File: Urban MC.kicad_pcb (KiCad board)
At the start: 4 copper layers, 167 x 104 mm, 79 parts, among them J1 Conn_01x02, J2 Conn_01x02, J3 Conn_01x03, J3 Screw_Terminal_01x02, J4 Conn_01x02, J4 Screw_Terminal_01x01, J5 Screw_Terminal_01x01, Q1 IQE022N06LM5CGSCATMA1, Q10 IQE022N06LM5CGSCATMA1, Q11 IQE022N06LM5CGSCATMA1, Q12 IQE022N06LM5CGSCATMA1, Q13 IQE022N06LM5CGSCATMA1, Q14 IQE022N06LM5CGSCATMA1, Q15 IQE022N06LM5CGSCATMA1, Q16 IQE022N06LM5CGSCATMA1, Q17 IQE022N06LM5CGSCATMA1, Q18 IQE022N06LM5CGSCATMA1, Q19 IQE022N06LM5CGSCATMA1, Q2 IQE022N06LM5CGSCATMA1, Q20 IQE022N06LM5CGSCATMA1, Q21 IQE022N06LM5CGSCATMA1, Q22 IQE022N06LM5CGSCATMA1, Q23 IQE022N06LM5CGSCATMA1, Q24 IQE022N06LM5CGSCATMA1, Q3 IQE022N06LM5CGSCATMA1, Q4 IQE022N06LM5CGSCATMA1, Q5 IQE022N06LM5CGSCATMA1, Q6 IQE022N06LM5CGSCATMA1, Q7 IQE022N06LM5CGSCATMA1, Q8 IQE022N06LM5CGSCATMA1, Q9 IQE022N06LM5CGSCATMA1, SW1 CAN_TERM, SW2 SW_Push, U1 MCP2561/2, U12 TJA1050, U2 MCP4725, U3 MCP2515-xSO, Y1 8MHz

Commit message: ready for mosfet feedback
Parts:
- removed the J2 at (137.7, 82.9)
- removed the J2 at (38.5, 151.0)
- removed the J3 at (58.3, 167.7)
- removed the J4 at (113.3, -58.2)
- removed the J4 at (102.4, 93.8)
- removed J5: Screw_Terminal_01x01, urban_mc_custom_footprints:WP-SHFU_7461100
- removed U12: TJA1050, Package_SO:SOIC-8_3.9x4.9mm_P1.27mm
- added J2: Conn_01x02, urban_mc_custom_footprints:CON_436500200_MOL, F.Cu at (116.8, 73.5)
- added J4: Conn_01x02, urban_mc_custom_footprints:TE_1-1986660-2, F.Cu at (95.2, 118.1)
- moved U4 210.6 mm to (102.9, 149.9)
- moved D4 204.6 mm to (105.4, 135.9)
- moved C14 203.7 mm to (121.0, 141.0)
- moved C15 202.4 mm to (121.9, 145.2)
- moved C16 202.4 mm to (121.9, 148.6)
- moved J1 154.1 mm to (127.0, 57.0)
- moved C5 94.1 mm to (212.1, 64.8)
- moved Q1 88.8 mm to (185.6, 62.3)
- moved Q3 88.8 mm to (191.7, 62.3)
- moved Q5 88.8 mm to (197.9, 62.3)
- moved Q7 88.8 mm to (204.0, 62.3)
- moved Q6 88.2 mm to (197.7, 69.8)
- moved Q8 88.2 mm to (203.9, 69.8)
- moved Q2 88.2 mm to (185.4, 69.8)
- moved Q4 88.2 mm to (191.6, 69.8)
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
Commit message: symbol changes and filled zone solution, still looking for more feedback
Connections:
- U3 pad 14: SI -> CS
- U3 pad 16: CS -> SI
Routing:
- net Net-(Q21-GATE): track 81.2 -> 79.7 mm

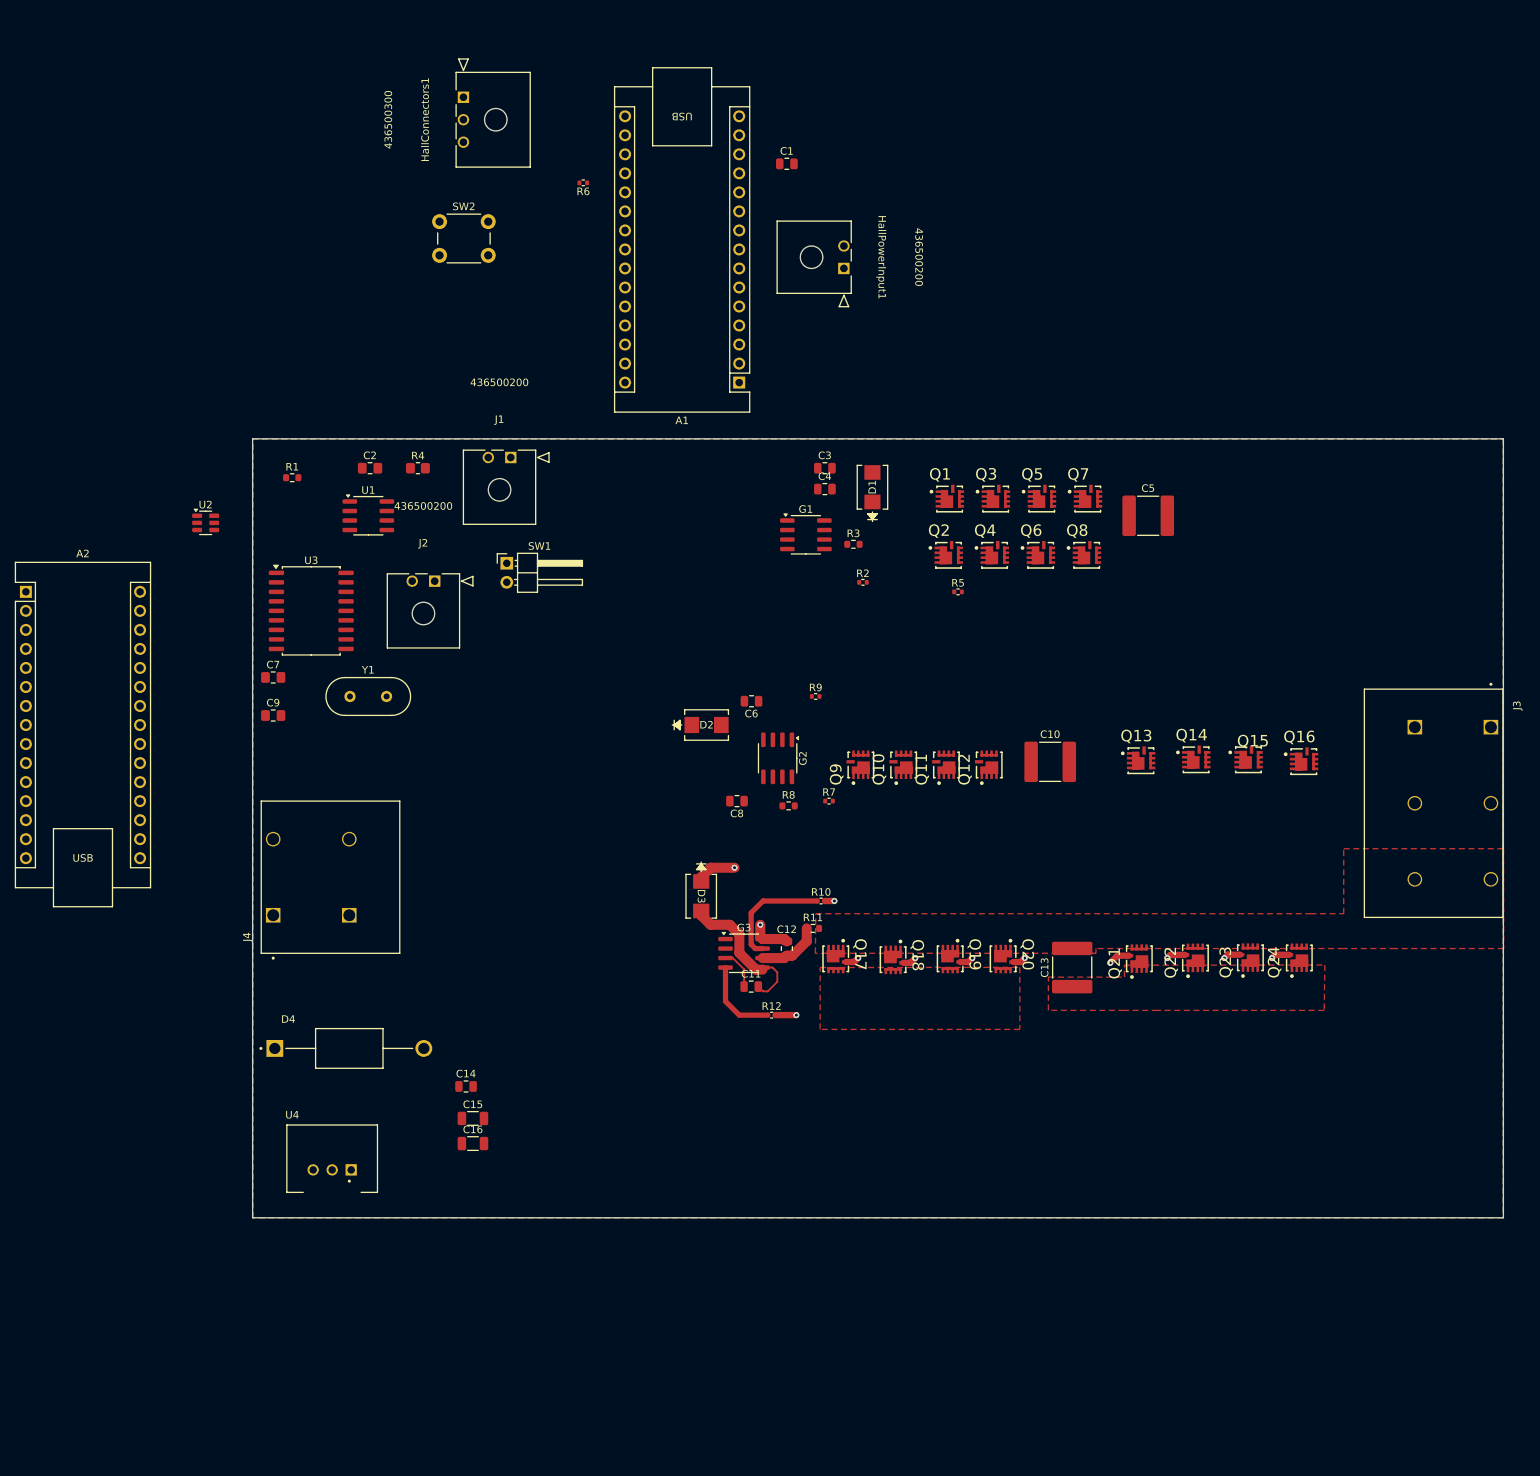
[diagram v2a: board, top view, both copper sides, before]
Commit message: duplicated mosfet section with connected filled zones
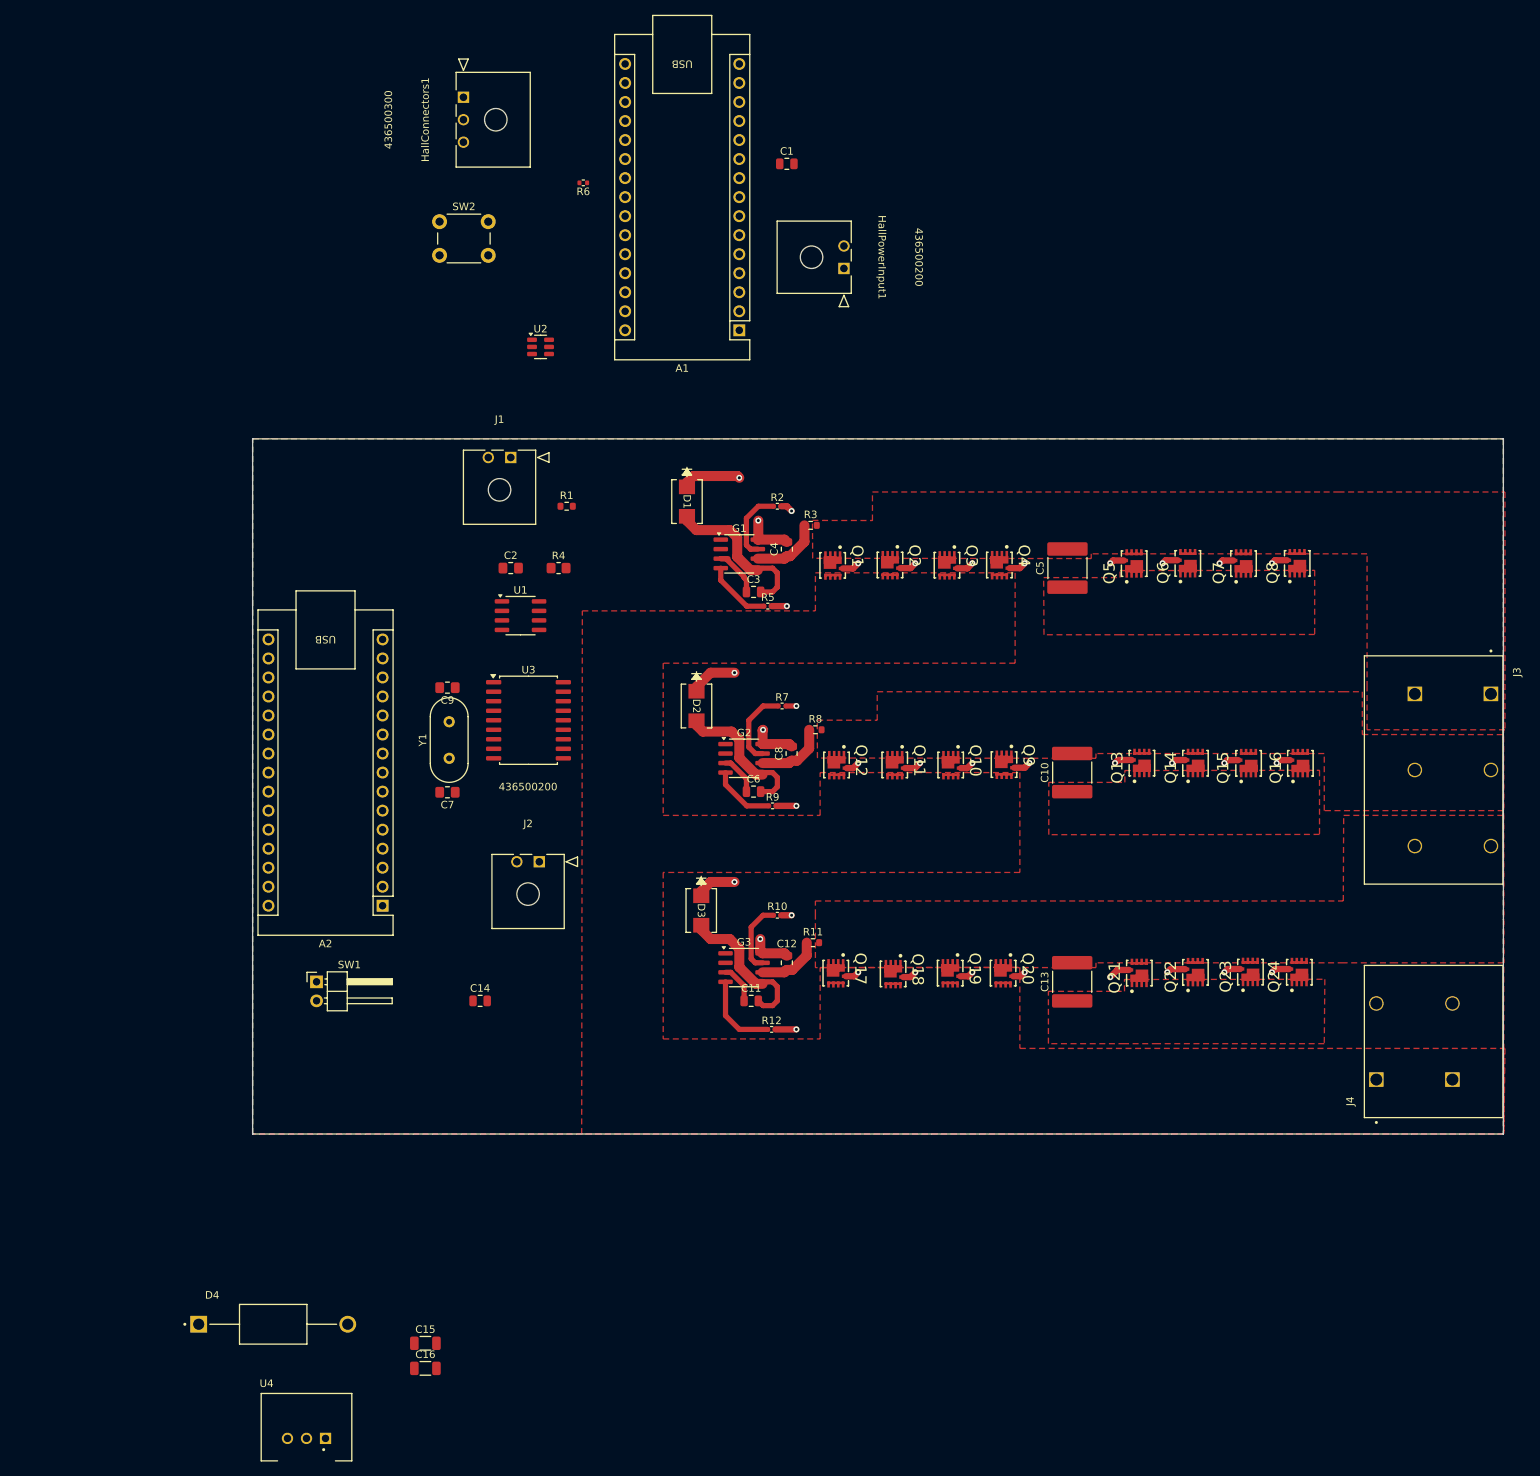
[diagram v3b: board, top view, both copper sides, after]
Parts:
- moved J4 148.9 mm to (242.5, 140.0)
- moved A2 63.4 mm to (109.9, 116.8), turned to 180 degrees
- moved SW1 61.4 mm to (101.0, 127.0)
- moved U2 50.5 mm to (130.9, 42.2)
- moved J2 40.0 mm to (130.8, 111.0)
- moved D4 38.2 mm to (95.2, 172.7)
- moved R1 36.8 mm to (134.4, 63.5)
- moved U4 36.0 mm to (99.4, 185.7)
- moved U3 32.5 mm to (129.3, 92.1)
- moved C16 30.7 mm to (115.6, 178.6)
- moved C15 30.7 mm to (115.6, 175.3)
- moved Q8 27.9 mm to (231.8, 71.1), turned to 90 degrees
- moved C7 27.9 mm to (118.5, 101.7), turned to 180 degrees
- moved R5 25.5 mm to (161.3, 76.8)
- moved D1 24.8 mm to (150.5, 62.9), turned to -90 degrees
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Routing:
- net Net-(Q5-GATE): track 0.00 -> 79.4 mm, vias 0 -> 5
- net Net-(Q13-GATE): track 0.00 -> 79.3 mm, vias 0 -> 5
- net Net-(Q10-GATE): track 0.00 -> 46.8 mm, vias 0 -> 5
- net Net-(Q1-GATE): track 0.00 -> 46.7 mm, vias 0 -> 5
- net +12V: track 20.1 -> 61.6 mm
- net Net-(G2-VB): track 0.00 -> 21.6 mm, vias 0 -> 2
- net Net-(G1-VB): track 0.00 -> 21.4 mm, vias 0 -> 2
- net GND: track 5.41 -> 17.9 mm
- net Net-(G2-HO): track 0.00 -> 10.5 mm
- net Net-(G1-HO): track 0.00 -> 9.61 mm
- net Net-(G2-VS): track 0.00 -> 9.53 mm
- net Net-(G1-VS): track 0.00 -> 9.35 mm
- net Net-(G1-LO): track 0.00 -> 8.82 mm
- net Net-(G2-LO): track 0.00 -> 8.56 mm
- net Net-(Q17-GATE): track 39.7 -> 45.9 mm
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- added copper zone on F.Cu, net Net-(J3-Pin_1)
- added copper zone on F.Cu, net Net-(J3-Pin_2)
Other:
- board size 167 x 104 mm -> 167 x 92.8 mm

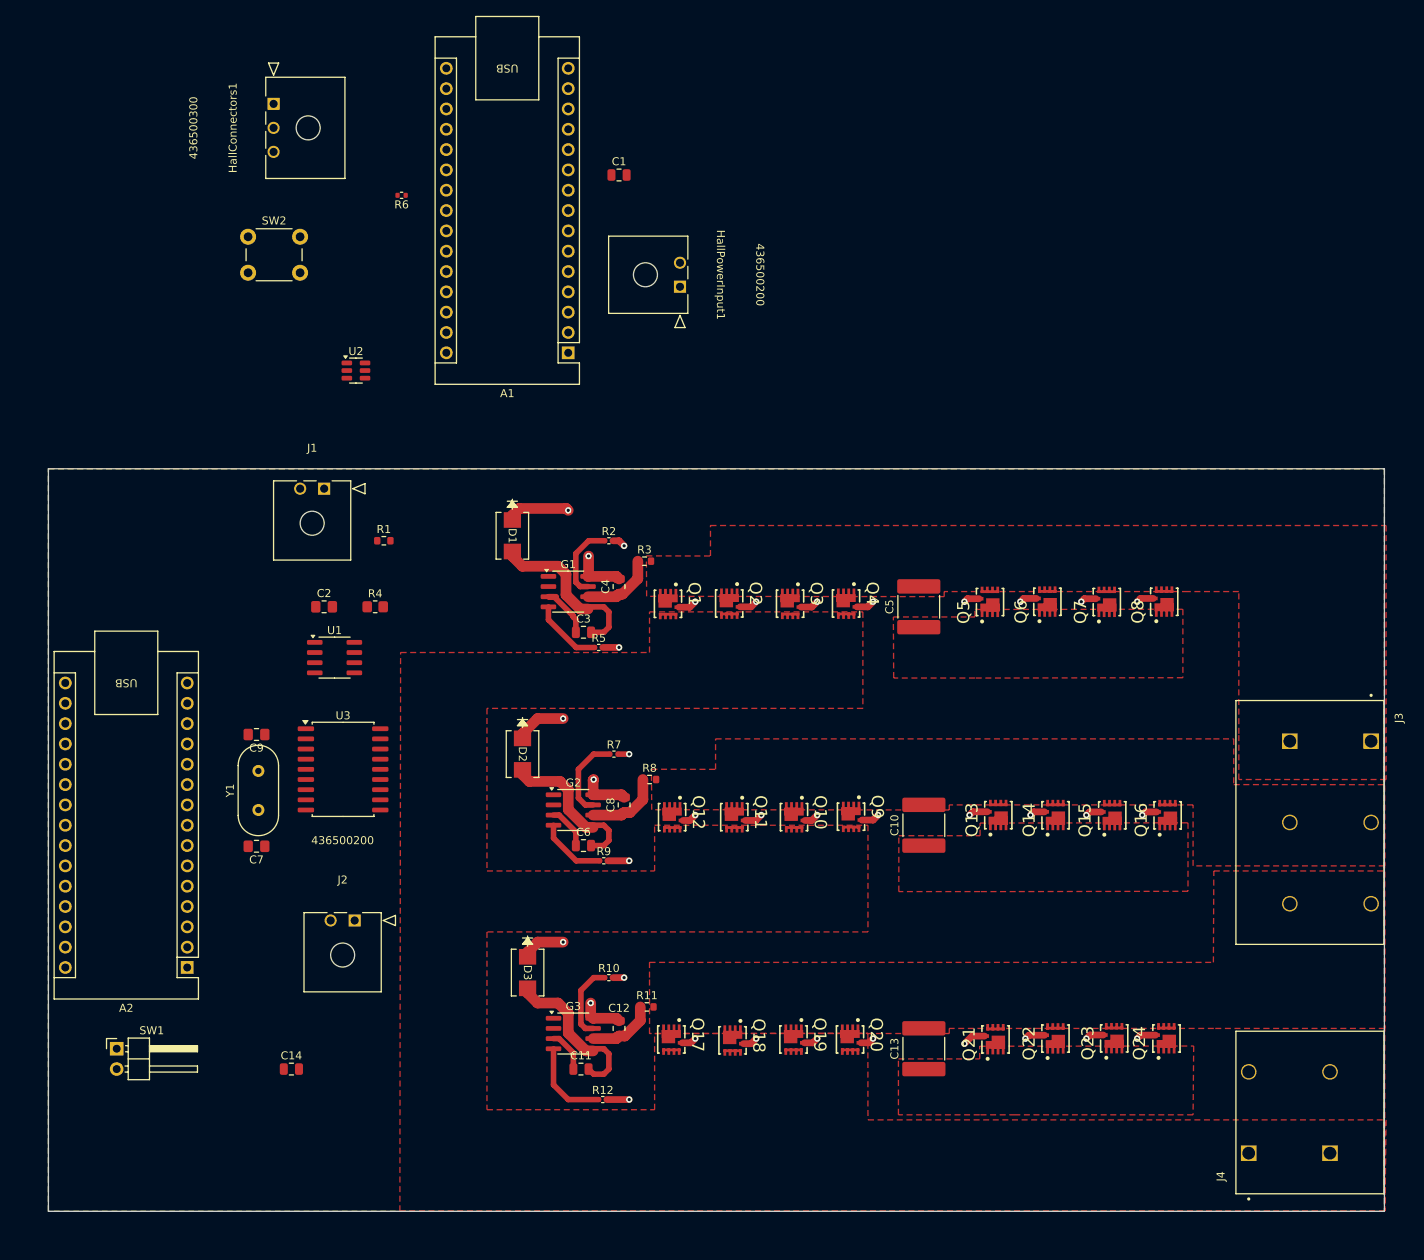
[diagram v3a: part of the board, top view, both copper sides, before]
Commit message: organized fet arduino circuit components
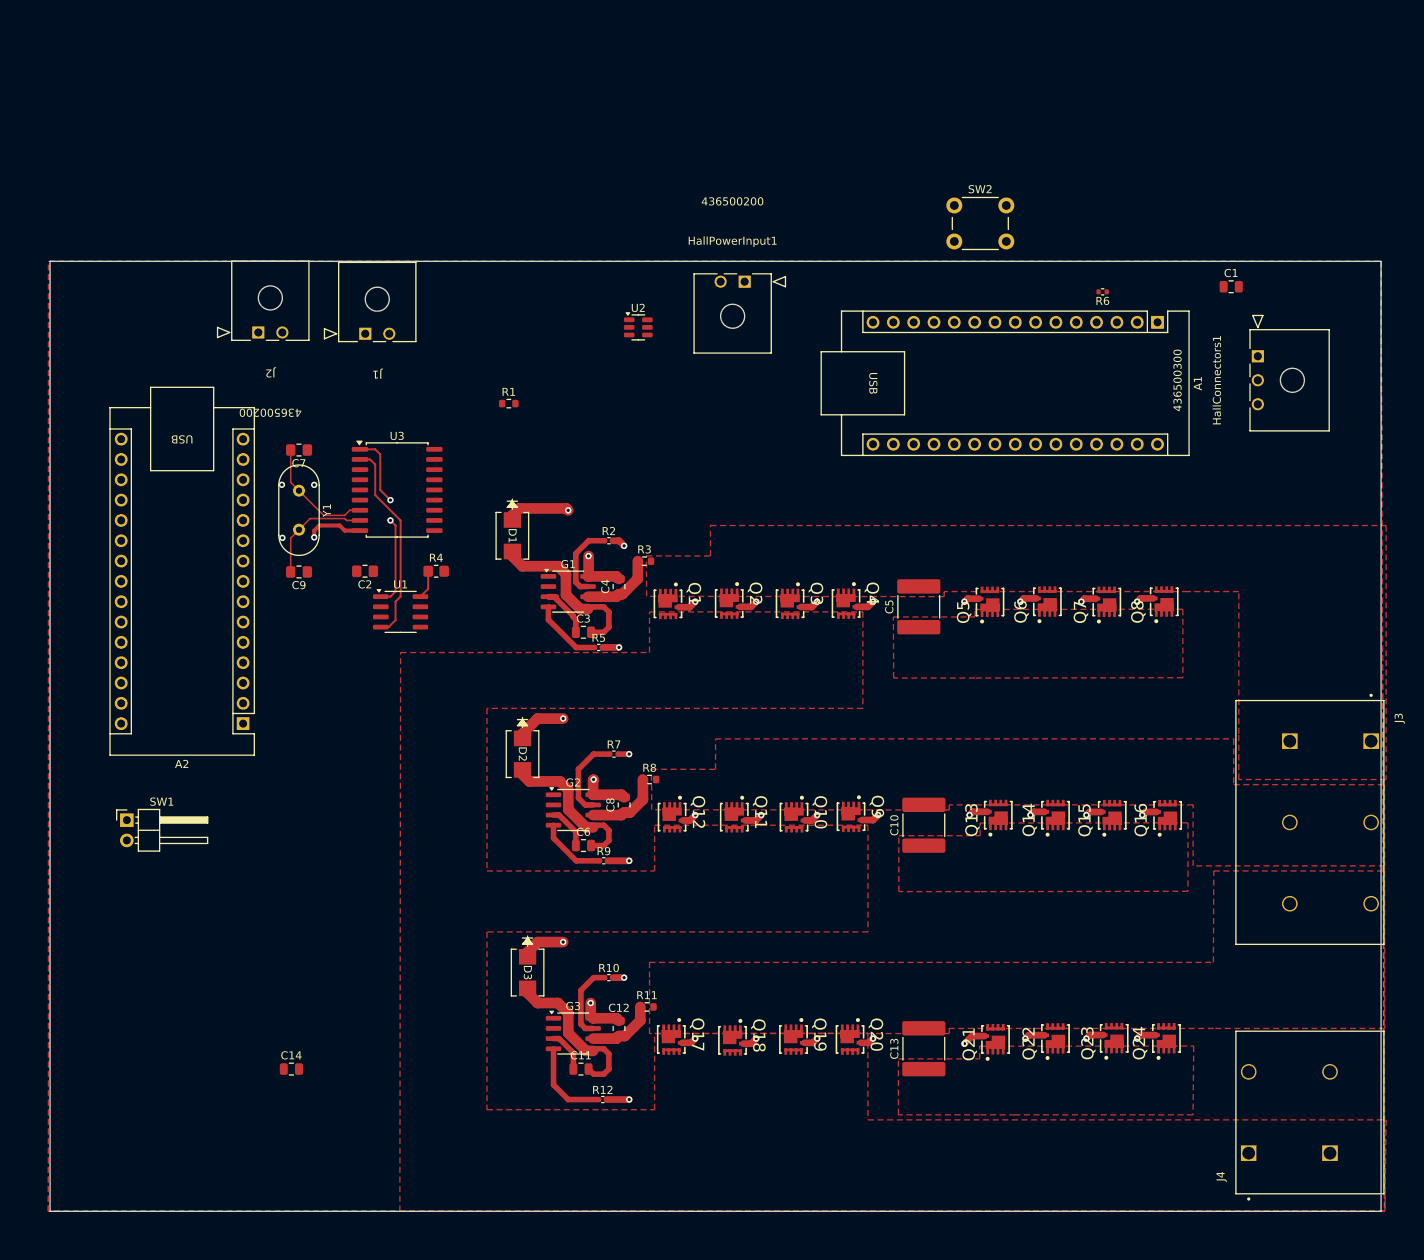
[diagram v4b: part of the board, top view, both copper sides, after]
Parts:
- moved HallConnectors1 127.0 mm to (243.7, 40.4)
- moved R6 88.5 mm to (224.3, 32.4)
- moved SW2 88.4 mm to (205.7, 21.6)
- moved C1 77.8 mm to (240.3, 31.8)
- moved J2 74.5 mm to (118.7, 37.5), turned to 180 degrees
- moved A1 73.8 mm to (231.1, 36.2), turned to -90 degrees
- moved C7 49.8 mm to (123.8, 52.2)
- moved Y1 40.2 mm to (123.8, 57.2), turned to -90 degrees
- moved U2 35.7 mm to (166.2, 36.8)
- moved U3 35.6 mm to (136.1, 57.1)
- moved A2 31.3 mm to (116.8, 86.4)
- moved SW1 28.6 mm to (102.3, 98.4)
- moved R1 23.2 mm to (150.1, 46.4)
- moved C9 21.0 mm to (123.8, 67.4)
- moved J1 20.0 mm to (132.1, 37.6), turned to 180 degrees
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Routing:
- net Net-(U1-RXD): track 0.00 -> 25.4 mm
- net Net-(U1-TXD): track 0.00 -> 22.8 mm, vias 0 -> 2
- net C+: track 0.00 -> 14.7 mm
- net C-: track 0.00 -> 14.0 mm
- net GND: track 17.9 -> 25.0 mm, vias 0 -> 4
- net Net-(U1-Rs): track 0.00 -> 3.58 mm
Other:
- board size 167 x 92.8 mm -> 166.4 x 118.7 mm
